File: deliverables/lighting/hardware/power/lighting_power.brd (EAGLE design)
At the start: 148.6 x 39 mm, 9 parts, among them J1 5055780671, J2 5055780671, J3 5055780671

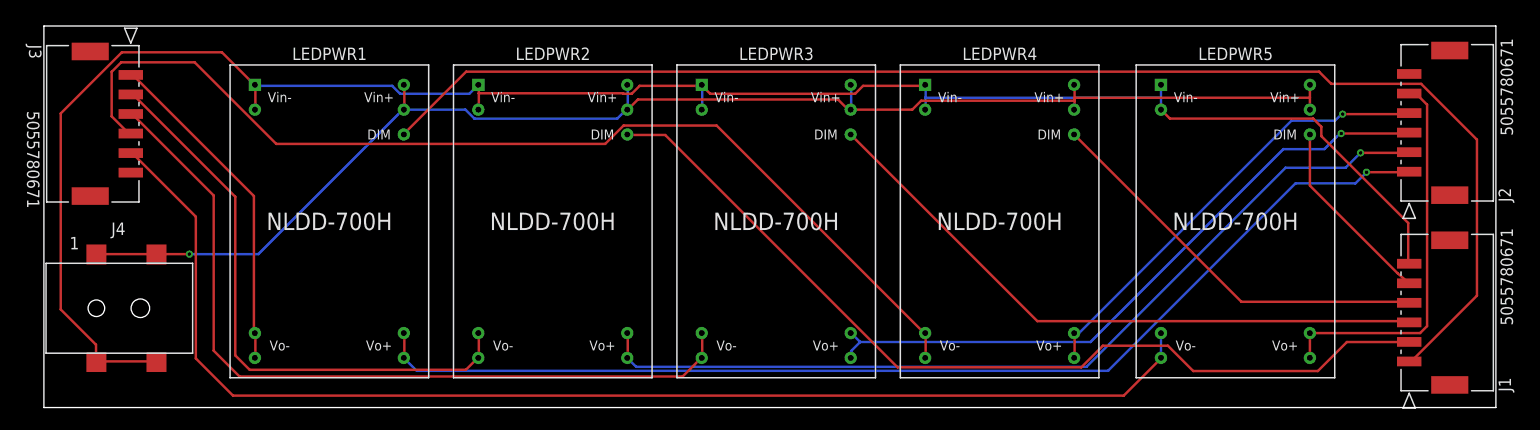
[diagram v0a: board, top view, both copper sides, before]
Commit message: Added Supporting Files for V0.2
SCH, BRD, and PNG for both
Also FBX models
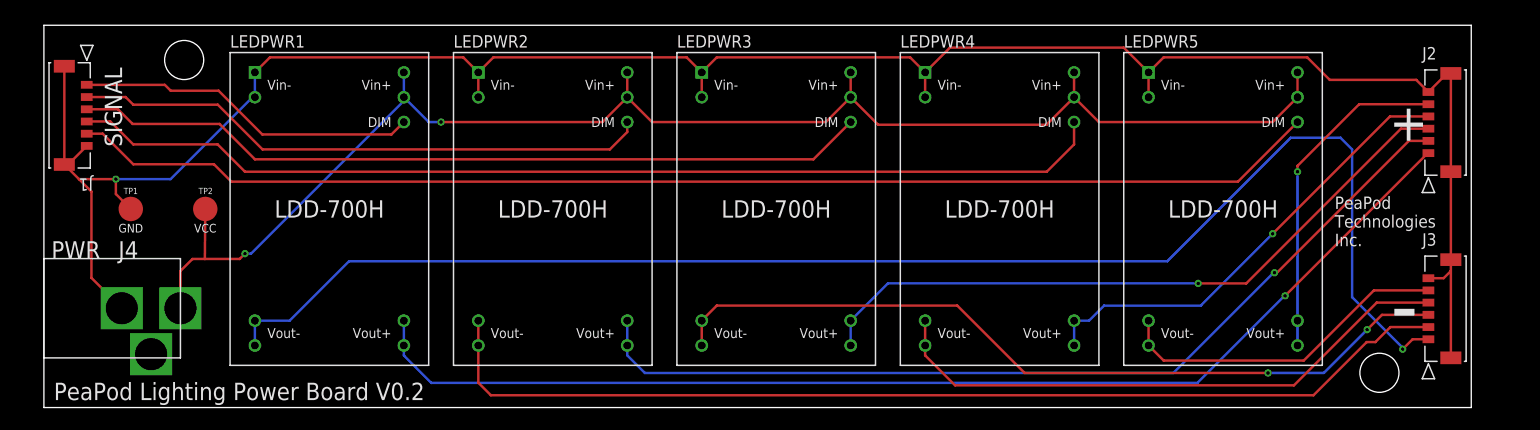
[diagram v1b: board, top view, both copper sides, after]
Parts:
- added TP1: GND, Test Point:TP_CIRCLE_2.5MM
- added TP2: VCC, Test Point:TP_CIRCLE_2.5MM
- J1, J2, J3: value 5055780671 -> MOLEX-MICROLOCK-6PIN; device Molex Micro-Lock PLUS 6-pin (90deg):CON_5055780671 -> Molex Micro-Lock PLUS 6-Pin 90deg:CON_5055670671
- J4: value (none) -> DCBARRELJACK; device Connector:694108106102 -> DC Barrel Jack (Locking):DCBARRELJACK
- LEDPWR1, LEDPWR2, LEDPWR3, LEDPWR4, LEDPWR5: value NLDD-700H -> LDD-700H; device MeanWell NLDD-700H:NLDD-700H -> MeanWell NLDD-H Series:NLDD-300~1000H
- moved J1 138.2 mm to (4.39, 94.0)
- moved J3 135.5 mm to (141.7, 67.9)
- moved J4 6.35 mm to (14.0, 71.1)
- moved J2 2.74 mm to (141.7, 87.0), turned to 270 degrees
- moved LEDPWR5 1.80 mm to (120.7, 81.3)
- moved LEDPWR1 1.27 mm to (29.2, 81.3)
- moved LEDPWR2 1.27 mm to (52.1, 81.3)
- moved LEDPWR3 1.27 mm to (74.9, 81.3)
- moved LEDPWR4 1.27 mm to (97.8, 81.3)
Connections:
- new net N$16: J4.P$2
- net GND: now also J1.7, J1.8, J2.6, J2.7, J2.8, J3.6, J3.7, J3.8, J4.P$3, TP1.P$1; no longer J4.2, J4.3
- net VCC: now also J4.P$1, TP2.P$1; no longer J4.1, J4.A1
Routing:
- net N$11: track 34.4 -> 148.7 mm, vias 0 -> 1
- net N$5: track 19.5 -> 128.4 mm
- net N$1: track 141.0 -> 35.1 mm
- net N$15: track 128.4 -> 34.8 mm
- net N$4: track 41.4 -> 106.6 mm
- net N$12: track 59.8 -> 107.0 mm
- net N$14: track 106.5 -> 59.8 mm
- net N$2: track 93.1 -> 59.3 mm
- net GND: track 199.4 -> 231.0 mm, vias 0 -> 1
- net N$3: track 65.1 -> 81.9 mm
- net VCC: track 145.3 -> 152.1 mm, vias 1 -> 2
- net N$10: track 39.8 -> 34.4 mm, vias 0 -> 1
- net N$6: track 114.4 -> 119.3 mm
- net N$7: track 92.1 -> 96.1 mm
- net N$8: track 68.4 -> 69.8 mm
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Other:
- board size 148.6 x 39 mm -> 146.1 x 39.1 mm
- board text added: "+"
- board text added: "-"
- board text added: "PWR"
- board text added: "PeaPod Lighting Power Board V0.2"
- board text added: "PeaPod Technologies Inc."
- board text added: "SIGNAL"
